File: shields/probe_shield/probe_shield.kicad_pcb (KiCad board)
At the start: 4 copper layers, 85 x 56 mm, 17 parts, among them IC1 NCP1117DT33T5G, J1 Probe Channel 0, J2 Probe Channel 1, J3 Probe Channel 2, J4 Probe Channel 3, J5 GPIO shield connector 40pin, J6 probe shield connector 20 or 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

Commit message: routing
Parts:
- moved J1 116.5 mm to (124.0, 105.0), turned to 30 degrees
- moved J2 100.1 mm to (137.0, 105.0), turned to 30 degrees
- moved J3 99.0 mm to (150.0, 105.0), turned to 30 degrees
- moved J4 84.3 mm to (163.0, 105.0), turned to 30 degrees
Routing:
- net /TMS|SWDIO_0: track 0.00 -> 88.2 mm
- net /TCK|SWDCLK_0: track 0.00 -> 85.4 mm
- net /TDO|SWO_0: track 0.00 -> 82.5 mm
- net /TDI|NC_0: track 0.00 -> 79.4 mm
- net /RST_0: track 0.00 -> 76.6 mm
- net /TMS|SWDIO_2: track 0.00 -> 57.4 mm
- net /TCK|SWDCLK_2: track 0.00 -> 54.6 mm
- net /TDO|SWO_2: track 0.00 -> 51.7 mm
- net /TDI|NC_2: track 0.00 -> 49.0 mm
- net /RST_2: track 0.00 -> 47.2 mm
- net GND: track 13.8 -> 42.1 mm, vias 2 -> 6
- net +3V3: track 39.0 -> 48.8 mm, vias 4 -> 8

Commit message: further work on probe shield layout
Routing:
- net /TMS|SWDIO_1: track 0.00 -> 84.4 mm, vias 0 -> 1
- net /TCK|SWDCLK_1: track 0.00 -> 82.0 mm, vias 0 -> 1
- net /TDO|SWO_1: track 0.00 -> 79.1 mm, vias 0 -> 1
- net /TDI|NC_1: track 0.00 -> 76.4 mm, vias 0 -> 1
- net /RST_1: track 0.00 -> 73.8 mm, vias 0 -> 1
- net /TMS|SWDIO_3: track 0.00 -> 47.8 mm, vias 0 -> 1
- net /TCK|SWDCLK_3: track 0.00 -> 45.1 mm, vias 0 -> 1
- net /TDO|SWO_3: track 0.00 -> 42.5 mm, vias 0 -> 1
- net /TDI|NC_3: track 0.00 -> 39.8 mm, vias 0 -> 1
- net /RST_3: track 0.00 -> 37.1 mm, vias 0 -> 1
- net +5V: track 20.0 -> 10.1 mm
- net /RST_0: track 76.6 -> 80.5 mm
- net /TDI|NC_2: track 49.0 -> 52.7 mm
- net /TDI|NC_0: track 79.4 -> 83.1 mm
- net /TDO|SWO_2: track 51.7 -> 55.3 mm
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- added copper zone on B.Cu, net +3V3
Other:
- board text added: "CH0"
- board text added: "CH1"
- board text added: "CH2"
- board text added: "CH3"
- board text added: "Probe"
- board text added: "probe shield rev. 0 probe-rs Thierry Kühni"

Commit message: added probe male connector, added 3d models and footprints for shield connectors
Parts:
- J5: footprint Connector_PinHeader_2.54mm:PinHeader_2x20_P2.54mm_Vertical -> hive:PinHeader_2x20_P2.54mm_Vertical_gpio_shield
- J6: value probe shield connector 20 or 26pin -> probe shield connector 26pin; footprint Connector_PinHeader_2.54mm:PinHeader_2x13_P2.54mm_Vertical -> hive:PinHeader_2x13_P2.54mm_Vertical_probe_shield_male
- renumbered LED1 to 3V3

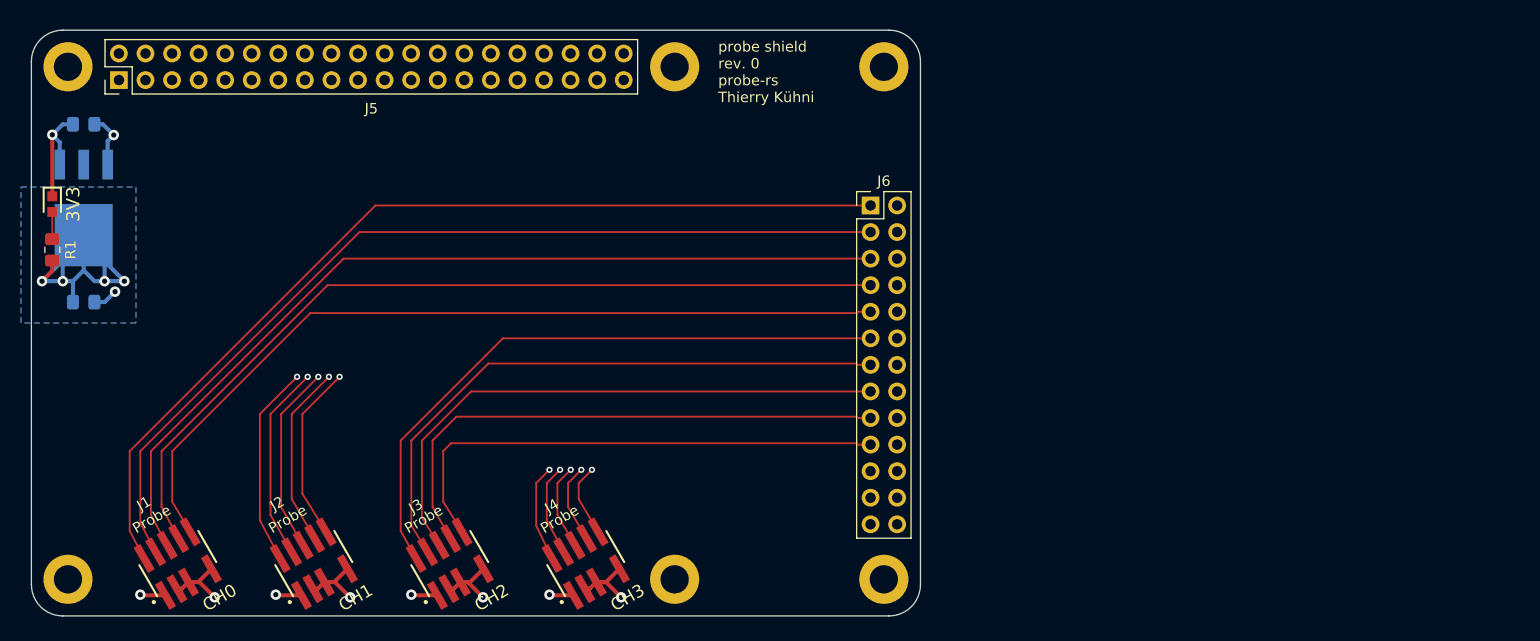
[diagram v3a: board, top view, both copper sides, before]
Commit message: length matching
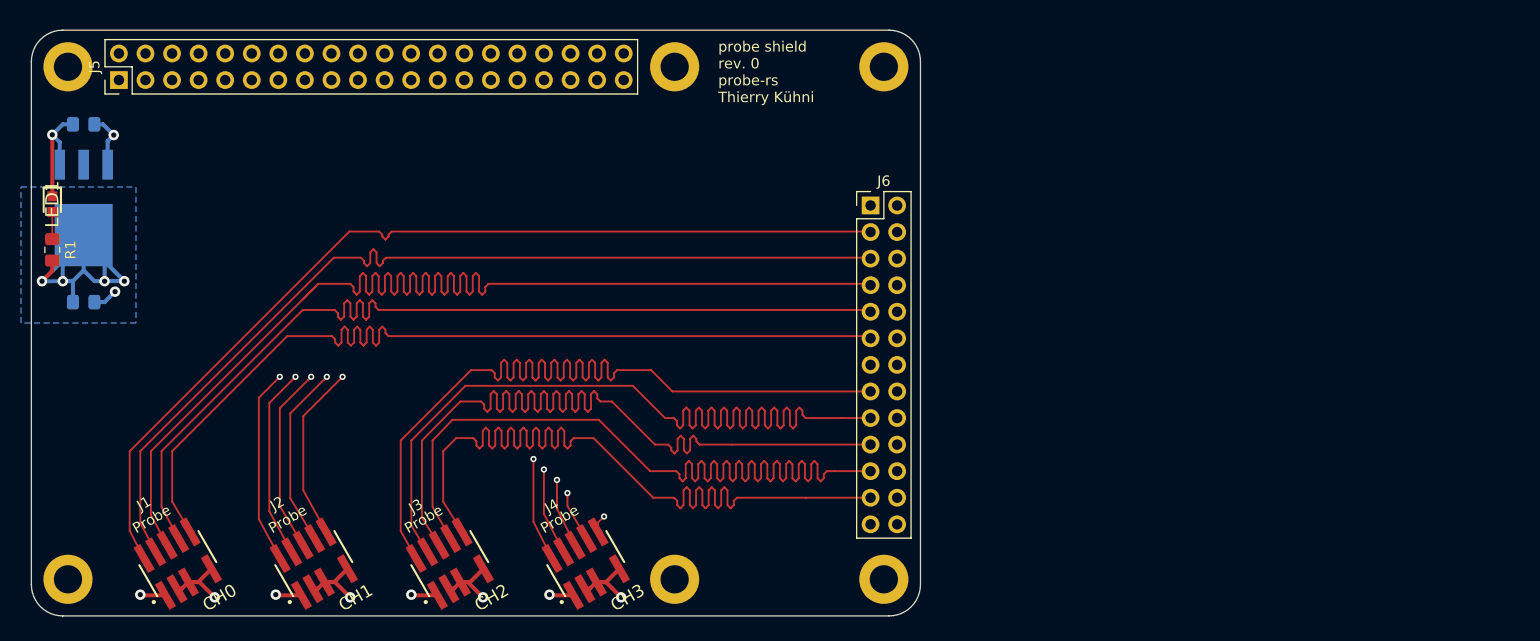
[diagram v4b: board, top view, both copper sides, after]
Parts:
- J5: footprint hive:PinHeader_2x20_P2.54mm_Vertical_gpio_shield -> Connector_PinHeader_2.54mm:PinHeader_2x20_P2.54mm_Vertical
- J6: footprint hive:PinHeader_2x13_P2.54mm_Vertical_probe_shield_male -> Connector_PinHeader_2.54mm:PinHeader_2x13_P2.54mm_Vertical
- R1: value 65 -> 195
- renumbered 3V3 to LED1
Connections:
- J6 pad 1: /TMS|SWDIO_0 -> GND
- J6 pad 10: /RST_1 -> /TDI|NC_1
- J6 pad 11: /TMS|SWDIO_2 -> /RST_0
- J6 pad 12: /TMS|SWDIO_3 -> /RST_1
- J6 pad 13: /TCK|SWDCLK_2 -> GND
- J6 pad 14: /TCK|SWDCLK_3 -> GND
- J6 pad 15: /TDO|SWO_2 -> /TMS|SWDIO_2
- J6 pad 16: /TDO|SWO_3 -> /TMS|SWDIO_3
- J6 pad 17: /TDI|NC_2 -> /TCK|SWDCLK_2
- J6 pad 18: /TDI|NC_3 -> /TCK|SWDCLK_3
- J6 pad 19: /RST_2 -> /TDO|SWO_2
- J6 pad 2: /TMS|SWDIO_1 -> GND
- J6 pad 20: /RST_3 -> /TDO|SWO_3
- J6 pad 21: GND -> /TDI|NC_2
- J6 pad 22: GND -> /TDI|NC_3
- J6 pad 23: GND -> /RST_2
- J6 pad 24: GND -> /RST_3
- J6 pad 3: /TCK|SWDCLK_0 -> /TMS|SWDIO_0
- J6 pad 4: /TCK|SWDCLK_1 -> /TMS|SWDIO_1
- J6 pad 5: /TDO|SWO_0 -> /TCK|SWDCLK_0
- J6 pad 6: /TDO|SWO_1 -> /TCK|SWDCLK_1
- J6 pad 7: /TDI|NC_0 -> /TDO|SWO_0
- J6 pad 8: /TDI|NC_1 -> /TDO|SWO_1
- J6 pad 9: /RST_0 -> /TDI|NC_0
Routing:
- net /RST_3: track 37.1 -> 91.0 mm
- net /TDI|NC_3: track 39.8 -> 91.0 mm
- net /TDO|SWO_3: track 42.5 -> 91.0 mm
- net /TCK|SWDCLK_3: track 45.1 -> 91.0 mm
- net /TMS|SWDIO_3: track 47.8 -> 91.0 mm
- net /RST_2: track 49.5 -> 91.0 mm
- net /TDI|NC_2: track 52.7 -> 91.0 mm
- net /TDO|SWO_0: track 85.8 -> 122.7 mm
- net /TDO|SWO_2: track 55.3 -> 91.0 mm
- net /TCK|SWDCLK_2: track 58.1 -> 91.0 mm
- net /TMS|SWDIO_2: track 60.6 -> 91.0 mm
- net /RST_1: track 73.8 -> 91.0 mm
- net /TDI|NC_1: track 76.4 -> 91.0 mm
- net /TDO|SWO_1: track 79.1 -> 91.0 mm
- net /RST_0: track 80.5 -> 91.0 mm
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
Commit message: probe shield 3d model update
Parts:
- J5: footprint Connector_PinHeader_2.54mm:PinHeader_2x20_P2.54mm_Vertical -> hive:PinHeader_2x20_P2.54mm_Vertical_gpio_shield
- J6: footprint Connector_PinHeader_2.54mm:PinHeader_2x13_P2.54mm_Vertical -> hive:PinHeader_2x13_P2.54mm_Vertical_probe_shield_male
- renumbered LED1 to 3V3

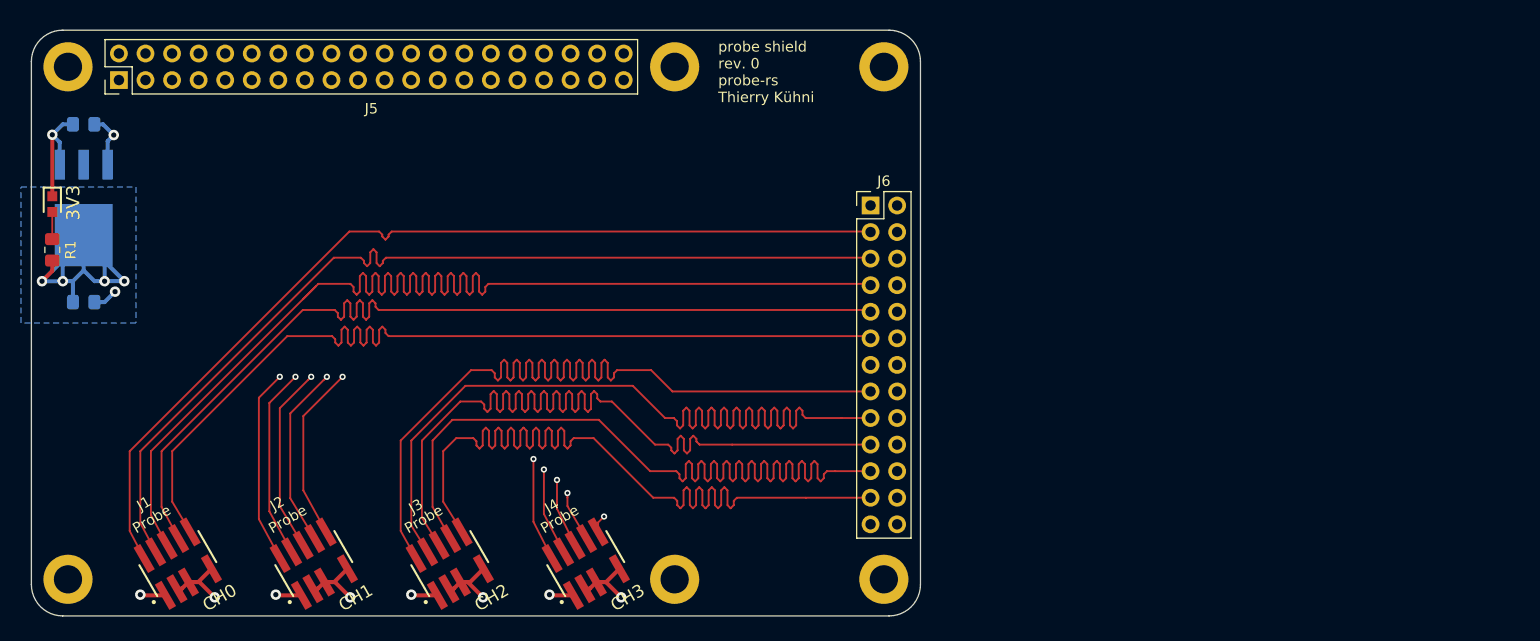
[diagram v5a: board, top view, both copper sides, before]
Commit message: updates on silkscreen, added 3d renders
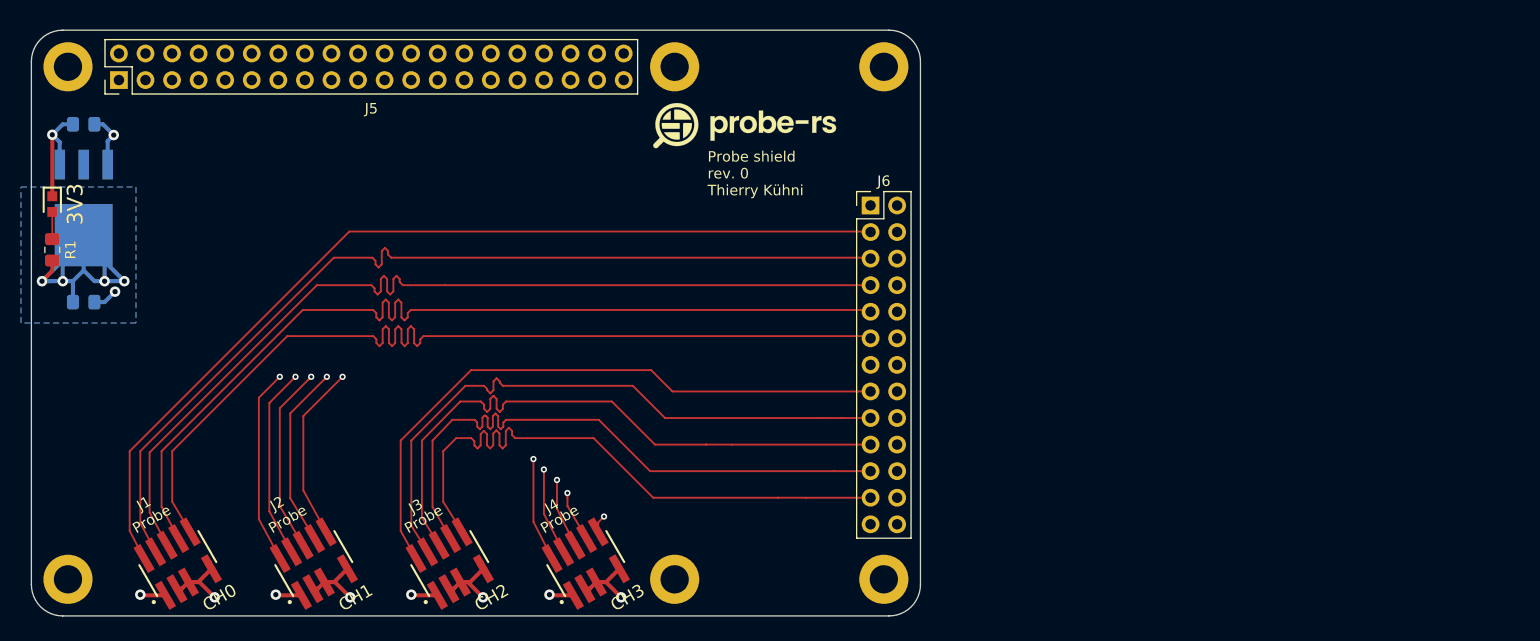
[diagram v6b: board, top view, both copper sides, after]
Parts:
- added G***: LOGO, hive:probe-rs-logo, F.Cu at (178.2, 63.1)
- renumbered 3V3 to LED1
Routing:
- net /RST_3: track 91.0 -> 48.0 mm
- net /TDO|SWO_3: track 91.0 -> 48.0 mm
- net /TDI|NC_3: track 91.0 -> 48.0 mm
- net /TCK|SWDCLK_3: track 91.0 -> 48.0 mm
- net /TMS|SWDIO_3: track 91.0 -> 48.0 mm
- net /TDO|SWO_0: track 122.7 -> 90.2 mm
- net /TMS|SWDIO_2: track 91.0 -> 60.2 mm
- net /TDI|NC_2: track 91.0 -> 60.3 mm
- net /TDO|SWO_2: track 91.0 -> 60.3 mm
- net /TCK|SWDCLK_2: track 91.0 -> 60.3 mm
- net /RST_2: track 91.0 -> 60.3 mm
- net /TDO|SWO_1: track 91.0 -> 85.0 mm
- net /RST_1: track 91.0 -> 85.0 mm
- net /TMS|SWDIO_1: track 91.0 -> 85.0 mm
- net /TDI|NC_1: track 91.0 -> 85.0 mm
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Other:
- board text added: "3V3"
- board text added: "Probe shield rev. 0 Thierry Kühni"
- board text removed: "probe shield rev. 0 probe-rs Thierry Kühni"

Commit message: Finished fabrication drawings
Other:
- board text added: "30°"
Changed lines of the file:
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@@
   (general
     (thickness 1.6)
-    (drawings 52)
+    (drawings 58)
     (tracks 551)
     (zones 0)
@@
       (effects (font (size 1 1) (thickness 0.15)))
     )
-    (fp_text value "probe shield connector 26pin" (at 6.77 15.24 90) (layer F.Fab)
+    (fp_text value "probe shield connector 26pin" (at -2.98 14.99 90) (layer F.Fab)
       (effects (font (size 1 1) (thickness 0.15)))
     )
@@
       (effects (font (size 1 1) (thickness 0.15)))
     )
-    (fp_text value "GPIO shield connector 40pin" (at 5.77 23.63) (layer F.Fab)
+    (fp_text value "GPIO shield connector 40pin" (at -2.48 24.13) (layer F.Fab)
       (effects (font (size 1 1) (thickness 0.15)))
     )
@@
     (fp_line (start 1.675 -0.925) (end 1.675 0.925) (layer F.CrtYd) (width 0.05))
     (fp_line (start -1.675 -0.925) (end 1.675 -0.925) (layer F.CrtYd) (width 0.05))
-    (fp_text user %R (at 0 0 90) (layer F.Fab)
+    (fp_text user %R (at 0 -1.75 90) (layer F.Fab)
       (effects (font (size 1.27 1.27) (thickness 0.254)))
     )
@@
     (fp_circle (center 0 0) (end 2.6 0) (layer F.CrtYd) (width 0.05))
     (fp_circle (center 0 0) (end 2.35 0) (layer Cmts.User) (width 0.15))
-    (fp_text user %R (at 0.3 0) (layer F.Fab)
+    (fp_text user %R (at 0.3 0) (layer F.Fab) hide
       (effects (font (size 1 1) (thickness 0.15)))
     )
@@
     (fp_circle (center 0 0) (end 2.6 0) (layer F.CrtYd) (width 0.05))
     (fp_circle (center 0 0) (end 2.35 0) (layer Cmts.User) (width 0.15))
-    (fp_text user %R (at 0.3 0) (layer F.Fab)
+    (fp_text user %R (at 0.3 0) (layer F.Fab) hide
       (effects (font (size 1 1) (thickness 0.15)))
     )
@@
     (fp_circle (center 0 0) (end 2.6 0) (layer F.CrtYd) (width 0.05))
     (fp_circle (center 0 0) (end 2.35 0) (layer Cmts.User) (width 0.15))
-    (fp_text user %R (at 0.3 0) (layer F.Fab)
+    (fp_text user %R (at 0.3 0) (layer F.Fab) hide
       (effects (font (size 1 1) (thickness 0.15)))
     )
@@
     (fp_circle (center 0 0) (end 2.6 0) (layer F.CrtYd) (width 0.05))
     (fp_circle (center 0 0) (end 2.35 0) (layer Cmts.User) (width 0.15))
-    (fp_text user %R (at 0.3 0) (layer F.Fab)
+    (fp_text user %R (at 0.3 0) (layer F.Fab) hide
       (effects (font (size 1 1) (thickness 0.15)))
     )
@@
     (fp_circle (center 0 0) (end 2.6 0) (layer F.CrtYd) (width 0.05))
     (fp_circle (center 0 0) (end 2.35 0) (layer Cmts.User) (width 0.15))
-    (fp_text user %R (at 0.3 0) (layer F.Fab)
+    (fp_text user %R (at 0.3 0) (layer F.Fab) hide
       (effects (font (size 1 1) (thickness 0.15)))
     )
@@
       (effects (font (size 1 1) (thickness 0.15)))
     )
-    (fp_text user %R (at 0.3 0) (layer F.Fab)
+    (fp_text user %R (at 0.3 0) (layer F.Fab) hide
       (effects (font (size 1 1) (thickness 0.15)))
     )
@@
     )
   )
+  (dimension 24 (width 0.15) (layer F.Fab)
+    (gr_text "24.000 mm" (at 199.8 98 270) (layer F.Fab)
+      (effects (font (size 1 1) (thickness 0.15)))
+    )
+    (feature1 (pts (xy 191.5 110) (xy 199.086421 110)))
+    (feature2 (pts (xy 191.5 86) (xy 199.086421 86)))
+    (crossbar (pts (xy 198.5 86) (xy 198.5 110)))
+    (arrow1a (pts (xy 198.5 110) (xy 197.913579 108.873496)))
+    (arrow1b (pts (xy 198.5 110) (xy 199.086421 108.873496)))
+    (arrow2a (pts (xy 198.5 86) (xy 197.913579 87.126504)))
+    (arrow2b (pts (xy 198.5 86) (xy 199.086421 87.126504)))
+  )
+  (dimension 29 (width 0.15) (layer F.Fab)
+    (gr_text "29.000 mm" (at 128 47.450001) (layer F.Fab)
+      (effects (font (size 1 1) (thickness 0.15)))
+    )
+    (feature1 (pts (xy 113.5 57.5) (xy 113.5 48.16358)))
+    (feature2 (pts (xy 142.5 57.5) (xy 142.5 48.16358)))
+    (crossbar (pts (xy 142.5 48.750001) (xy 113.5 48.750001)))
+    (arrow1a (pts (xy 113.5 48.750001) (xy 114.626504 48.16358)))
+    (arrow1b (pts (xy 113.5 48.750001) (xy 114.626504 49.336422)))
+    (arrow2a (pts (xy 142.5 48.750001) (xy 141.373496 48.16358)))
+    (arrow2b (pts (xy 142.5 48.750001) (xy 141.373496 49.336422)))
+  )
+  (dimension 3.5 (width 0.15) (layer F.Fab)
+    (gr_text "3.500 mm" (at 111.75 46.5) (layer F.Fab)
+      (effects (font (size 1 1) (thickness 0.15)) (justify left))
+    )
+    (feature1 (pts (xy 110 57.5) (xy 110 48.163579)))
+    (feature2 (pts (xy 113.5 57.5) (xy 113.5 48.163579)))
+    (crossbar (pts (xy 113.5 48.75) (xy 110 48.75)))
+    (arrow1a (pts (xy 110 48.75) (xy 111.126504 48.163579)))
+    (arrow1b (pts (xy 110 48.75) (xy 111.126504 49.336421)))
+    (arrow2a (pts (xy 113.5 48.75) (xy 112.373496 48.163579)))
+    (arrow2b (pts (xy 113.5 48.75) (xy 112.373496 49.336421)))
+  )
+  (gr_text 30° (at 139.5 107.5) (layer F.Fab)
+    (effects (font (size 1 1) (thickness 0.15)))
+  )
+  (gr_arc (start 135.107869 108.072734) (end 141.499999 107.750001) (angle -25.68257441) (layer F.Fab) (width 0.15))
+  (dimension 13 (width 0.15) (layer F.Fab)
+    (gr_text "13.000 mm" (at 156.5 114.8) (layer F.Fab)
+      (effects (font (size 1 1) (thickness 0.15)))
+    )
+    (feature1 (pts (xy 163 105) (xy 163 114.086421)))
+    (feature2 (pts (xy 150 105) (xy 150 114.086421)))
+    (crossbar (pts (xy 150 113.5) (xy 163 113.5)))
+    (arrow1a (pts (xy 163 113.5) (xy 161.873496 114.086421)))
+    (arrow1b (pts (xy 163 113.5) (xy 161.873496 112.913579)))
+    (arrow2a (pts (xy 150 113.5) (xy 151.126504 114.086421)))
+    (arrow2b (pts (xy 150 113.5) (xy 151.126504 112.913579)))
+  )
+  (dimension 13 (width 0.15) (layer F.Fab)
+    (gr_text "13.000 mm" (at 143.5 114.8) (layer F.Fab)
+      (effects (font (size 1 1) (thickness 0.15)))
+    )
+    (feature1 (pts (xy 150 105) (xy 150 114.086421)))
+    (feature2 (pts (xy 137 105) (xy 137 114.086421)))
+    (crossbar (pts (xy 137 113.5) (xy 150 113.5)))
+    (arrow1a (pts (xy 150 113.5) (xy 148.873496 114.086421)))
+    (arrow1b (pts (xy 150 113.5) (xy 148.873496 112.913579)))
+    (arrow2a (pts (xy 137 113.5) (xy 138.126504 114.086421)))
+    (arrow2b (pts (xy 137 113.5) (xy 138.126504 112.913579)))
+  )
+  (dimension 13 (width 0.15) (layer F.Fab)
+    (gr_text "13.000 mm" (at 130.5 114.8) (layer F.Fab)
+      (effects (font (size 1 1) (thickness 0.15)))
+    )
+    (feature1 (pts (xy 137 105) (xy 137 114.086421)))
+    (feature2 (pts (xy 124 105) (xy 124 114.086421)))
+    (crossbar (pts (xy 124 113.5) (xy 137 113.5)))
+    (arrow1a (pts (xy 137 113.5) (xy 135.873496 114.086421)))
+    (arrow1b (pts (xy 137 113.5) (xy 135.873496 112.913579)))
+    (arrow2a (pts (xy 124 113.5) (xy 125.126504 114.086421)))
+    (arrow2b (pts (xy 124 113.5) (xy 125.126504 112.913579)))
+  )
+  (dimension 14 (width 0.15) (layer F.Fab)
+    (gr_text "14.000 mm" (at 117 114.8) (layer F.Fab)
+      (effects (font (size 1 1) (thickness 0.15)))
+    )
+    (feature1 (pts (xy 110 105) (xy 110 114.086421)))
+    (feature2 (pts (xy 124 105) (xy 124 114.086421)))
+    (crossbar (pts (xy 124 113.5) (xy 110 113.5)))
+    (arrow1a (pts (xy 110 113.5) (xy 111.126504 112.913579)))
+    (arrow1b (pts (xy 110 113.5) (xy 111.126504 114.086421)))
+    (arrow2a (pts (xy 124 113.5) (xy 122.873496 112.913579)))
+    (arrow2b (pts (xy 124 113.5) (xy 122.873496 114.086421)))
+  )
   (gr_text 3V3 (at 114.191 70.63 90) (layer F.SilkS)
     (effects (font (size 1.5 1.5) (thickness 0.3)))
@@
   (gr_line (start 113 110) (end 192 110) (layer Edge.Cuts) (width 0.05))
   (gr_line (start 113 110) (end 192 110) (layer B.Fab) (width 0.05))
-  (dimension 20 (width 0.15) (layer F.Fab)
-    (gr_text "20.000 mm" (at 181.5 114.3) (layer F.Fab)
-      (effects (font (size 1 1) (thickness 0.15)))
-    )
-    (feature1 (pts (xy 191.5 106.5) (xy 191.5 113.586421)))
-    (feature2 (pts (xy 171.5 106.5) (xy 171.5 113.586421)))
-    (crossbar (pts (xy 171.5 113) (xy 191.5 113)))
-    (arrow1a (pts (xy 191.5 113) (xy 190.373496 113.586421)))
-    (arrow1b (pts (xy 191.5 113) (xy 190.373496 112.413579)))
-    (arrow2a (pts (xy 171.5 113) (xy 172.626504 113.586421)))
-    (arrow2b (pts (xy 171.5 113) (xy 172.626504 112.413579)))
-  )
-  (dimension 58 (width 0.15) (layer F.Fab)
-    (gr_text "58.000 mm" (at 142.5 114.3) (layer F.Fab)
-      (effects (font (size 1 1) (thickness 0.15)))
-    )
-    (feature1 (pts (xy 171.5 106.5) (xy 171.5 113.586421)))
-    (feature2 (pts (xy 113.5 106.5) (xy 113.5 113.586421)))
-    (crossbar (pts (xy 113.5 113) (xy 171.5 113)))
-    (arrow1a (pts (xy 171.5 113) (xy 170.373496 113.586421)))
-    (arrow1b (pts (xy 171.5 113) (xy 170.373496 112.413579)))
-    (arrow2a (pts (xy 113.5 113) (xy 114.626504 113.586421)))
-    (arrow2b (pts (xy 113.5 113) (xy 114.626504 112.413579)))
-  )
   (dimension 3.5 (width 0.15) (layer F.Fab)
-    (gr_text "3.500 mm" (at 111.75 114.3) (layer F.Fab)
-      (effects (font (size 1 1) (thickness 0.15)))
-    )
-    (feature1 (pts (xy 113.5 106.5) (xy 113.5 113.586421)))
-    (feature2 (pts (xy 110 106.5) (xy 110 113.586421)))
-    (crossbar (pts (xy 110 113) (xy 113.5 113)))
-    (arrow1a (pts (xy 113.5 113) (xy 112.373496 113.586421)))
-    (arrow1b (pts (xy 113.5 113) (xy 112.373496 112.413579)))
-    (arrow2a (pts (xy 110 113) (xy 111.126504 113.586421)))
-    (arrow2b (pts (xy 110 113) (xy 111.126504 112.413579)))
-  )
-  (dimension 3.5 (width 0.15) (layer F.Fab)
-    (gr_text "3.500 mm" (at 103.2 108.25 90) (layer F.Fab)
-      (effects (font (size 1 1) (thickness 0.15)))
+    (gr_text "3.500 mm" (at 102 108.25 90) (layer F.Fab)
+      (effects (font (size 1 1) (thickness 0.15)) (justify left))
     )
     (feature1 (pts (xy 113.5 110) (xy 103.913579 110)))
